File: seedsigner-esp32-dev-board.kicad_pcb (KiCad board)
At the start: 2 copper layers, 70 x 78 mm, 11 parts, among them J1 Conn_01x06, J2 Conn_01x08, U1 ESP32-S2-SAOLA-1M, U2 OV_CAMERA, U3 RASPBERRY_PI_3_MODEL_B+

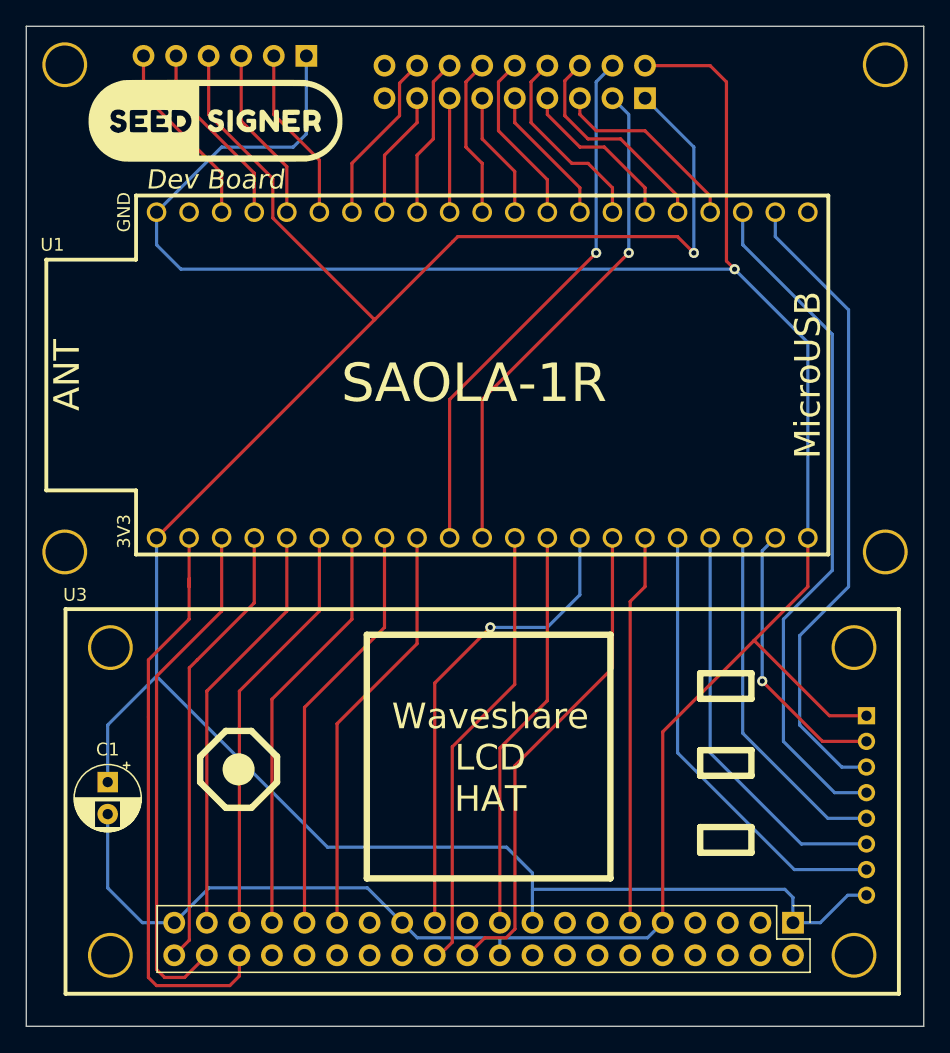
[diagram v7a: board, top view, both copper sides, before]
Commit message: add gerbers and fix RESET and PWM pin
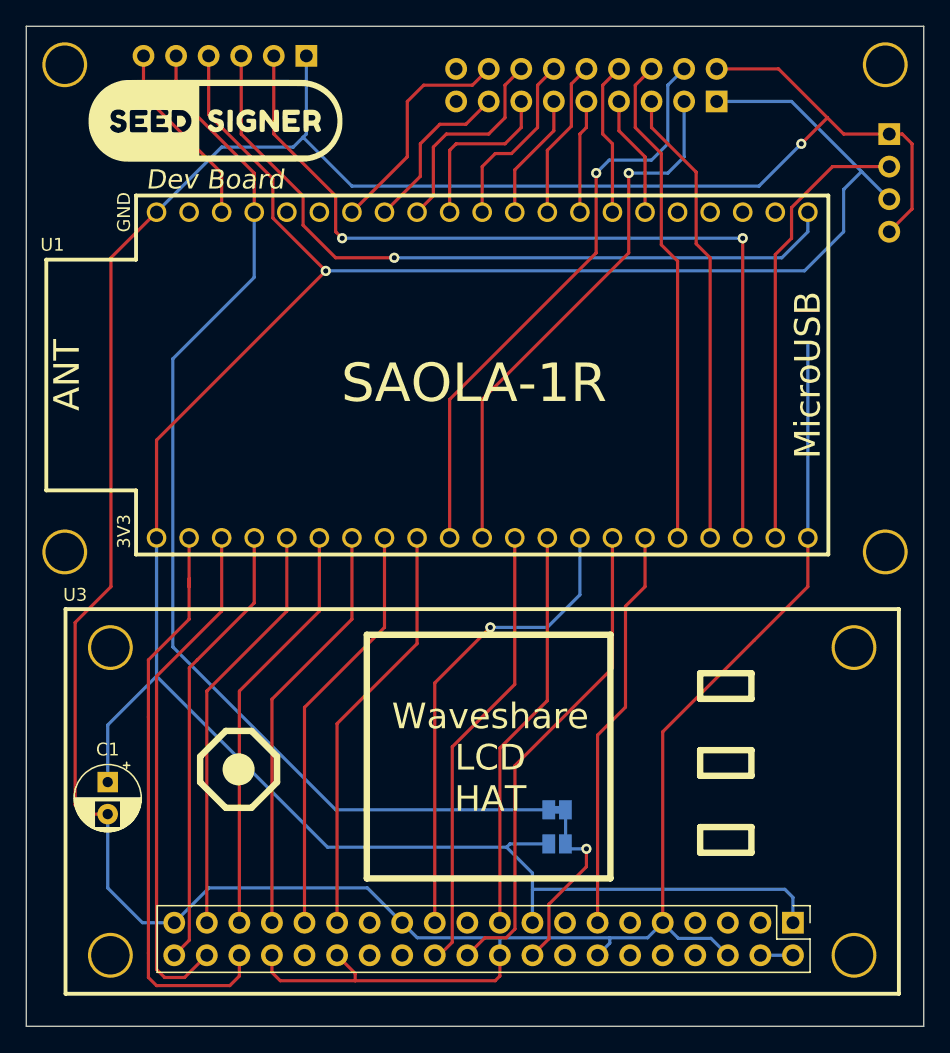
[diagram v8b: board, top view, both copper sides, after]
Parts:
- added JP1: Jumper_2_Bridged, Jumper:SolderJumper-2_P1.3mm_Bridged_Pad1.0x1.5mm, B.Cu at (41.4, -16.9)
- added JP2: Jumper_2_Open, Jumper:SolderJumper-2_P1.3mm_Open_Pad1.0x1.5mm, B.Cu at (41.4, -14.2)
- added LOGO2: CORN-LOGO, SeedSigner:corn-logo, B.Cu at (61.0, -19.1)
- J2: value Conn_01x08 -> Conn_01x04; footprint Connector_PinSocket_2.00mm:PinSocket_1x08_P2.00mm_Vertical -> Connector_PinHeader_2.54mm:PinHeader_1x04_P2.54mm_Vertical
- moved J2 45.4 mm to (67.3, -69.6)
- moved U2 5.59 mm to (43.7, -73.4)
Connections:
- net /IO_TRIG renamed /BACKLIGHT_PWM
- J1 pad 2: /TX -> /TX1
- J1 pad 3: /RX -> /RX1
- J2 pad 3: /XTRA1 -> +3.3V
- J2 pad 4: /XTRA2 -> GND
- U1 pad 15: /XTRA5 -> /HREF
- U1 pad 16: /XTRA4 -> /VSYNC
- U1 pad 17: /XTRA3 -> /TX1
- U1 pad 18: unconnected-(U1-Pad18) -> /RX1
- U1 pad 19: /XTRA1 -> unconnected-(U1-Pad19)
- U1 pad 20: /XTRA2 -> unconnected-(U1-Pad20)
- U1 pad 21: /VSYNC -> unconnected-(U1-Pad21)
- U1 pad 26: /HREF -> /PSRAM_NO_USE
- U1 pad RX: /RX -> unconnected-(U1-PadRX)
- U1 pad TX: /TX -> unconnected-(U1-PadTX)
- U3 pad 11: /RST -> unconnected-(U3-Pad11)
- U3 pad 13: unconnected-(U3-Pad13) -> /RST
- U3 pad 18: unconnected-(U3-Pad18) -> /BACKLIGHT
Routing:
- net /BACKLIGHT_PWM: track 14.7 -> 85.8 mm
- net /TX1: track 0.00 -> 71.0 mm, vias 0 -> 2
- net GND: track 214.5 -> 278.3 mm
- net /RX1: track 0.00 -> 58.0 mm, vias 0 -> 1
- net /XTRA2: track 53.9 -> 0.00 mm
- net /XTRA1: track 50.5 -> 0.00 mm
- net /XTRA5: track 35.3 -> 0.00 mm
- net /XTRA4: track 31.9 -> 0.00 mm
- net /XTRA3: track 27.6 -> 0.00 mm
- net /HREF: track 17.0 -> 38.5 mm
- net /VSYNC: track 15.3 -> 35.9 mm
- net +3.3V: track 181.1 -> 196.5 mm
- net /BACKLIGHT: track 0.00 -> 14.5 mm, vias 0 -> 1
- net /RX: track 13.7 -> 0.00 mm
- net /TX: track 13.7 -> 0.00 mm
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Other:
- board text added: "PWR"
- board text removed: "15"
- board text removed: "16"
- board text removed: "17"
- board text removed: "19"
- board text removed: "20"
